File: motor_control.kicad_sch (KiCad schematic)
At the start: 79 parts, among them J6 Screw_Terminal_01x04, J7 Screw_Terminal_01x02, Q11 2V7002, Q5 BSS138, Q7 SiS443DN, T15 I_SNS, T16 D_FB, T17 D_PWM2, T18 D_PWM1, T19 VC_OUT, T20 V_LDSNS, T22 VC_CMP, T23 VC_REF, T25 DRV_EN, T26 DRV_SF, T27 SF_Q, T28 SF_TRG, T29 SF_CLR, T30 ENC_B, T31 ENC_A, U10 LM4040DBZ-2.5, U11 MCP6561x-LT, U12 ZXTR2105F, U14 ACS722xLCTR-10AB, U18 MC33HB2002, U7 74LVC2G14, U8 74LVC1G123

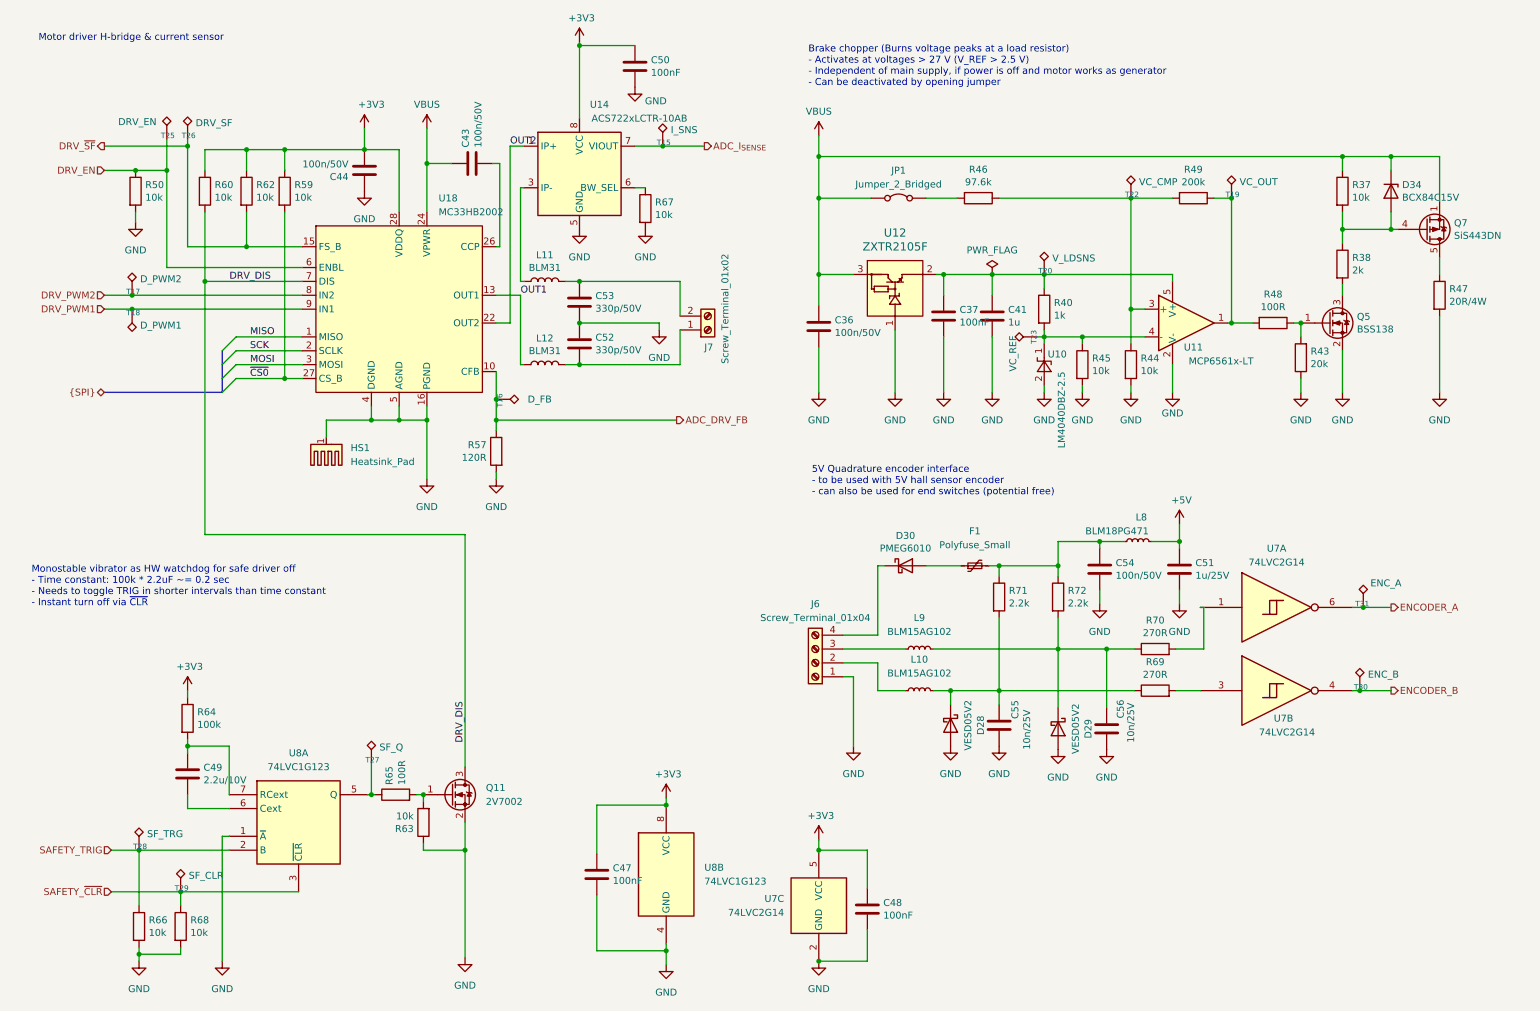
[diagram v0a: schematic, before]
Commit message: Simplified design (Old version switched to hodor-max)
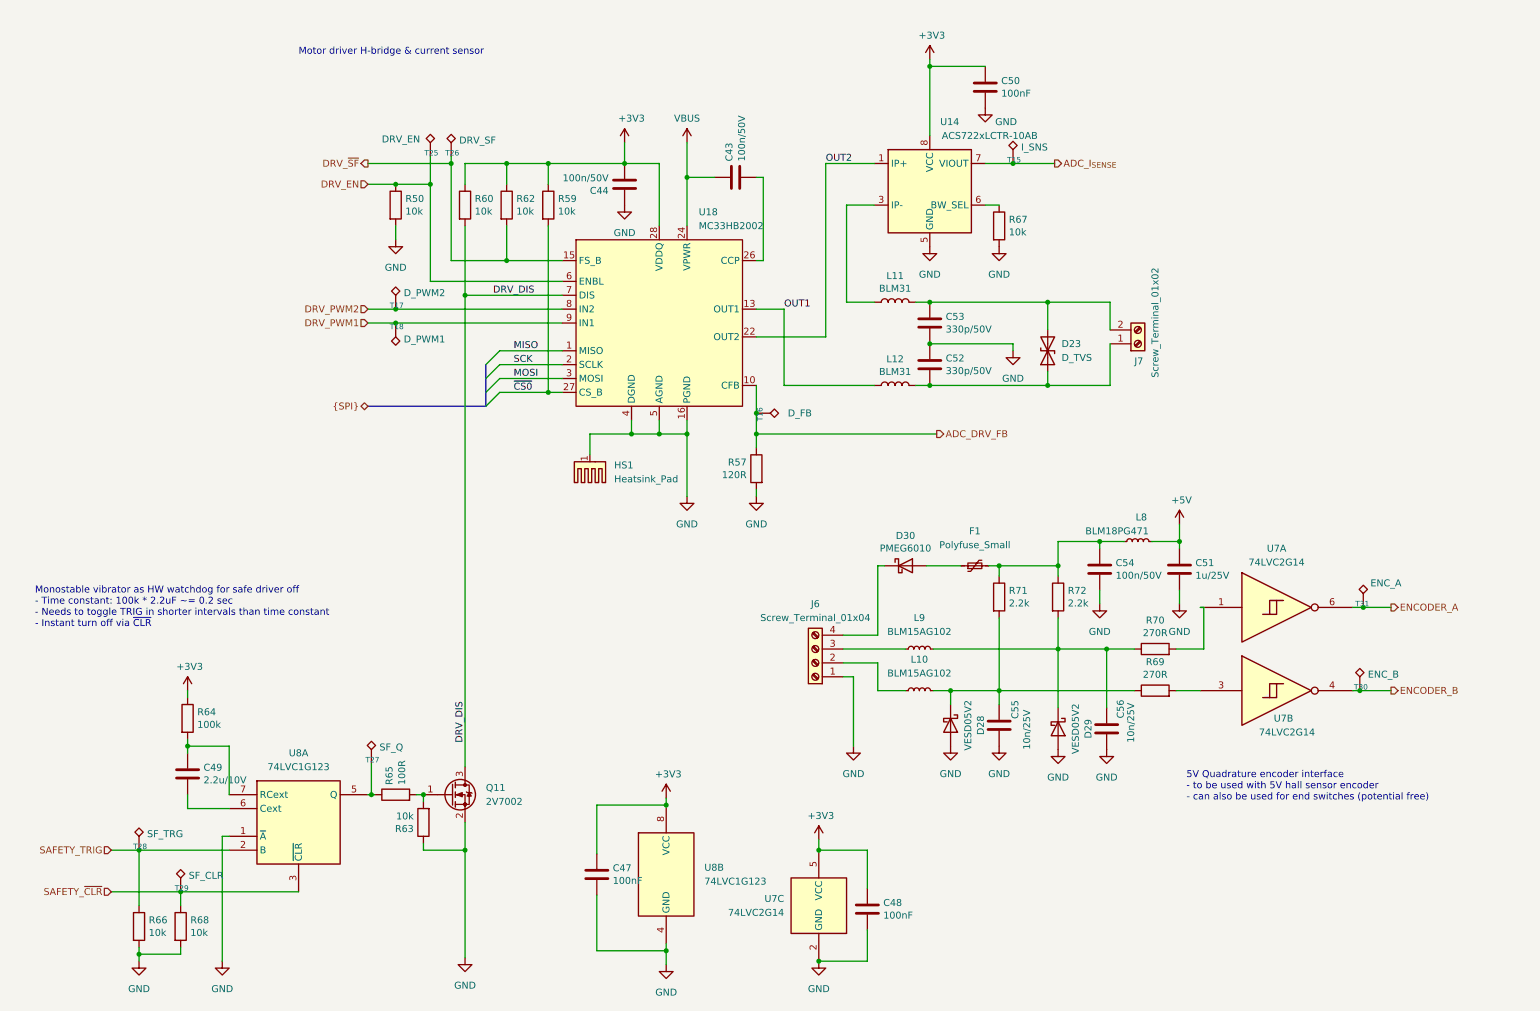
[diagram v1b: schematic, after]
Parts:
- removed C36: 100n/50V, Capacitor_SMD:C_0603_1608Metric, symbol Device:C
- removed C37: 100nF, Capacitor_SMD:C_0402_1005Metric, symbol Device:C
- removed C41: 1u, Capacitor_SMD:C_0402_1005Metric, symbol Device:C
- removed D34: BCX84C15V, Diode_SMD:D_SOD-523, symbol Device:D_Zener
- removed JP1: Jumper_2_Bridged, Jumper:SolderJumper-2_P1.3mm_Bridged_Pad1.0x1.5mm, symbol Jumper:Jumper_2_Bridged
- removed Q5: BSS138, Package_TO_SOT_SMD:SOT-23, symbol Transistor_FET:BSS138
- removed Q7: SiS443DN, Package_SO:Vishay_PowerPAK_1212-8_Single, symbol Transistor_FET:SiS443DN
- removed R37, R44, R45: 10k, Resistor_SMD:R_0402_1005Metric, symbol Device:R
- removed R38: 2k, Resistor_SMD:R_0805_2012Metric, symbol Device:R
- removed R40: 1k, Resistor_SMD:R_0402_1005Metric, symbol Device:R
- removed R43: 20k, Resistor_SMD:R_0402_1005Metric, symbol Device:R
- removed R46: 97.6k, Resistor_SMD:R_0402_1005Metric, symbol Device:R
- removed R47: 20R/4W, Resistor_SMD:R_2816_7142Metric, symbol Device:R
- removed R48: 100R, Resistor_SMD:R_0402_1005Metric, symbol Device:R
- removed R49: 200k, Resistor_SMD:R_0402_1005Metric, symbol Device:R
- removed T19: VC_OUT, TestPoint:TestPoint_Pad_D1.0mm, symbol Connector:TestPoint_Alt
- removed T20: V_LDSNS, TestPoint:TestPoint_Pad_D1.0mm, symbol Connector:TestPoint_Alt
- removed T22: VC_CMP, TestPoint:TestPoint_Pad_D1.0mm, symbol Connector:TestPoint_Alt
- removed T23: VC_REF, TestPoint:TestPoint_Pad_D1.0mm, symbol Connector:TestPoint_Alt
- removed U10: LM4040DBZ-2.5, Package_TO_SOT_SMD:SOT-23, symbol Reference_Voltage:LM4040DBZ-2.5
- removed U11: MCP6561x-LT, Package_TO_SOT_SMD:SOT-353_SC-70-5, symbol Comparator:MCP6561x-LT
- removed U12: ZXTR2105F, Package_TO_SOT_SMD:SOT-23, symbol hodor_custom_parts:ZXTR2105F
- added D23: D_TVS, Diode_SMD:D_SMB, symbol Device:D_TVS
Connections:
- net at C53.1, J7.2 (Pin_2), L11.2: now also D23.2 (A2)
- net at C52.2, J7.1 (Pin_1), L12.2: now also D23.1 (A1)
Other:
- note removed: "Brake chopper (Burns voltage peaks at a load resistor) - Activates at voltages > 27 V (V_REF > 2.5 V) - Independent of main supply, if power is off and motor works as generator - Can be deactivated by opening jumper"
- moved on the sheet: C43, C44, C50, C52, C53, HS1, J7, L11, L12, R50, R57, R59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

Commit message: Finalized Layout
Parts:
- C29: renamed from C49; value 2.2u/10V -> 2.2u/25V; footprint Capacitor_SMD:C_0603_1608Metric -> Capacitor_SMD:C_0805_2012Metric
- renumbered C47 to C28, C44 to C39, C43 to C40, C50 to C41, C48 to C42, C52 to C43, C53 to C44, C55 to C45, C56 to C46, C54 to C47, C51 to C48, D23 to D14, D28 to D15, D29 to D16, D30 to D17, F1 to F2, J7 to J6, J6 to J7, L11 to L10, L9 to L11, L10 to L12, L8 to L13, L12 to L9, Q11 to Q3, R66 to R19, R64 to R20, R68 to R23, R63 to R24, R65 to R25, R60 to R29, R62 to R30, R57 to R31, R59 to R32, R50 to R33, R67 to R34, R71 to R35, R69 to R36, R70 to R37, R72 to R38, T16 to T12, T15 to T13, T28 to T14, T29 to T15, T27 to T16, T31 to T19, T25 to T20, T30 to T21, T26 to T22, U18 to U10, U14 to U11, U7 to U12
